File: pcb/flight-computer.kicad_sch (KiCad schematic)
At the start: 48 parts, among them J1 MicroSD Slot, J2 USB_C_Receptacle_USB2.0_16P, SW1 SW_Push, SW2 SW_Push, U1 RP2040, U2 W25Q16JVSS, U3 USBLC6-2SC6, Y1 12MHz

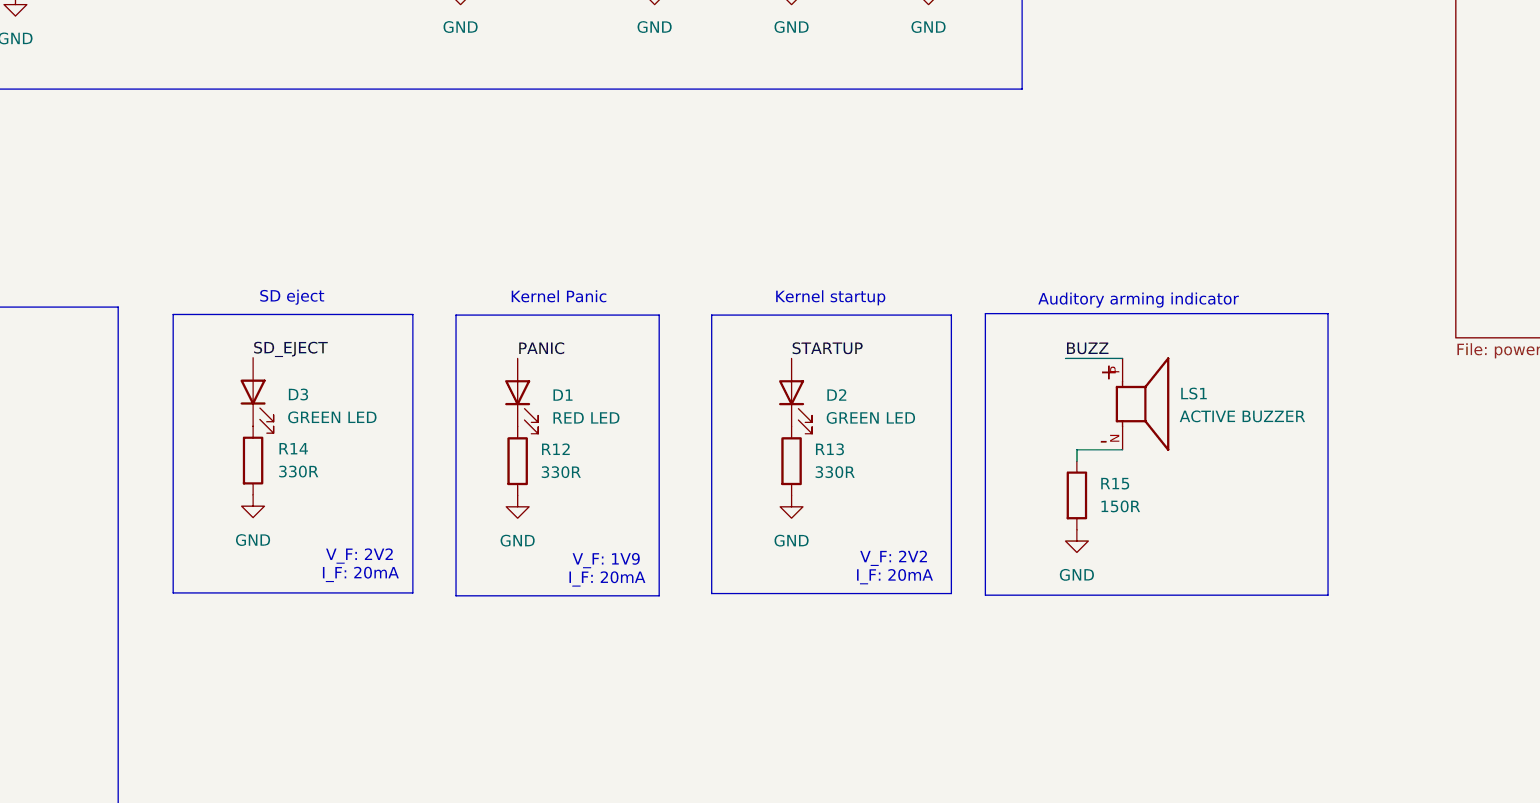
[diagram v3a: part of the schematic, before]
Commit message: Added MOSFET to drive the buzzer.
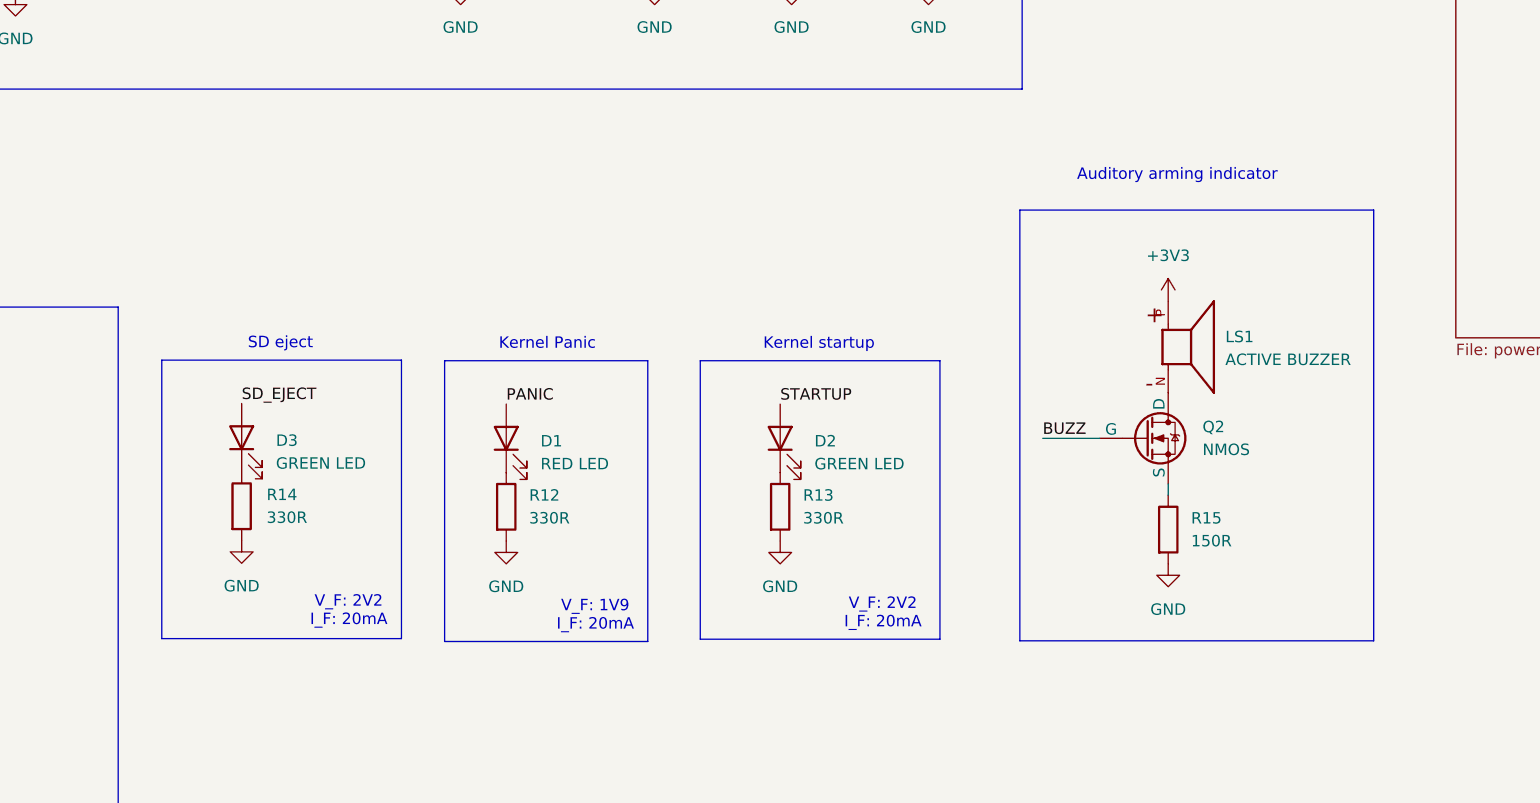
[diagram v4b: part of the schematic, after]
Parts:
- added Q2: NMOS, Package_TO_SOT_SMD:SOT-23-3, symbol Simulation_SPICE:NMOS
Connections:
- net +3V3: now also LS1.P
- net BUZZ: now also Q2.1 (G); no longer LS1.P
- net at R15.1: now also Q2.2 (S); no longer LS1.N
- new net: LS1.N, Q2.3 (D)
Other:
- moved on the sheet: D1, D2, D3, LS1, R12, R13, R14, R15

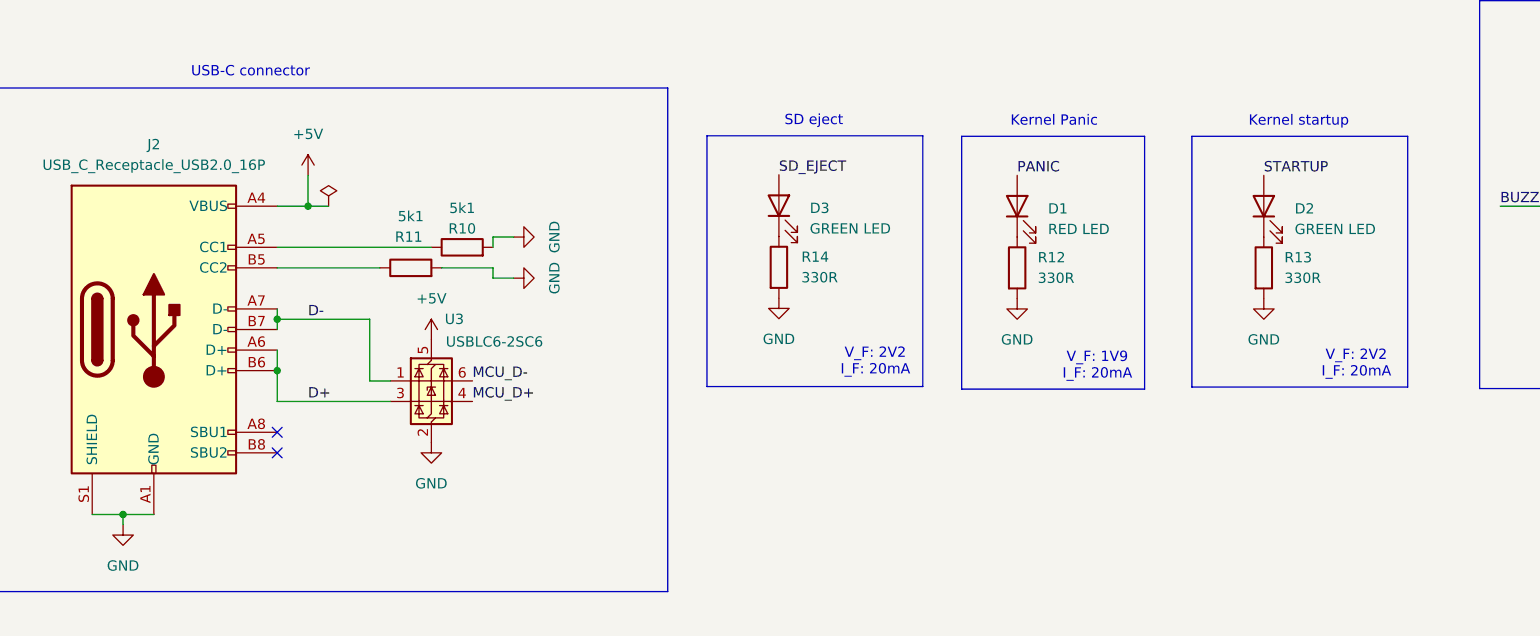
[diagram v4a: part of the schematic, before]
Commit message: Removed DRC errors on schematic by adding power flags.
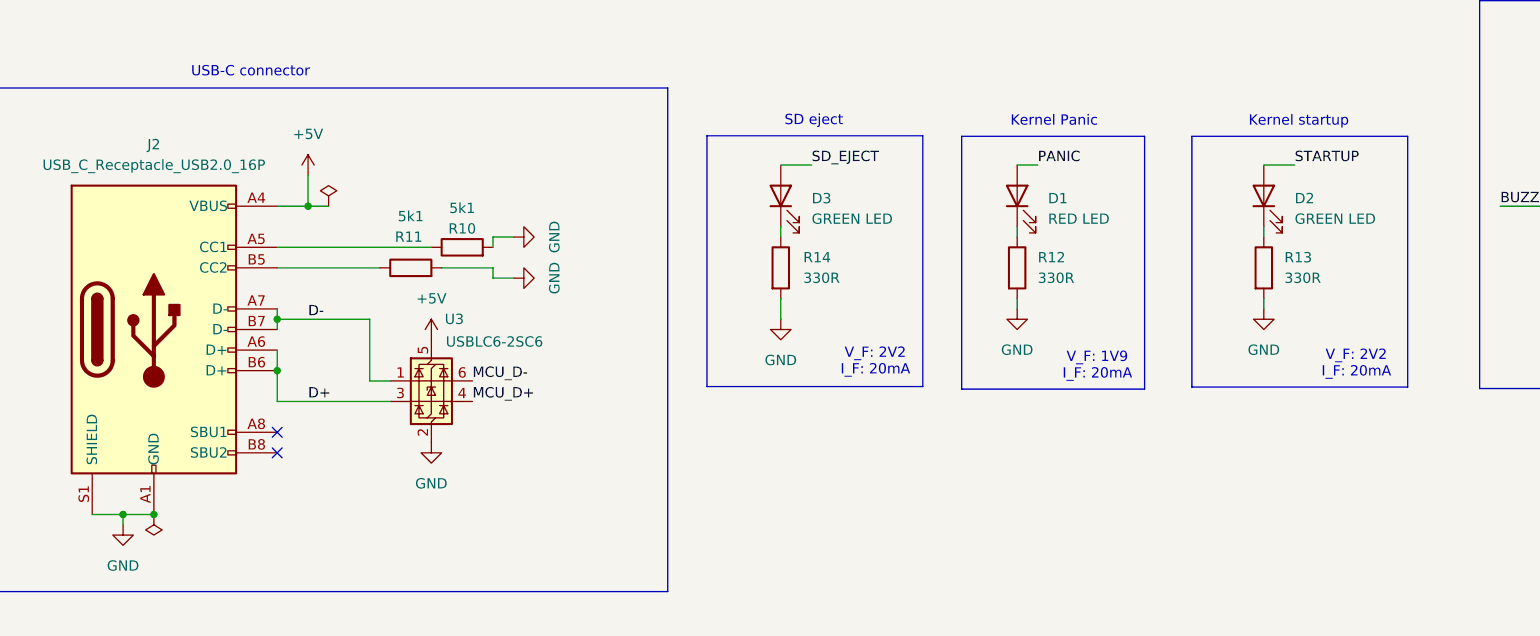
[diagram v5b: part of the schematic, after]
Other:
- moved on the sheet: D1, D2, D3
